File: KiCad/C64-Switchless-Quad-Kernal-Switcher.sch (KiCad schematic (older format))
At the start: 9 parts, among them J1 Pinlist_12pin, J2 Pinlist_12pin, J3 27C256_28PDIP, J4 Wireconnections, U1 ATtiny85-20PU

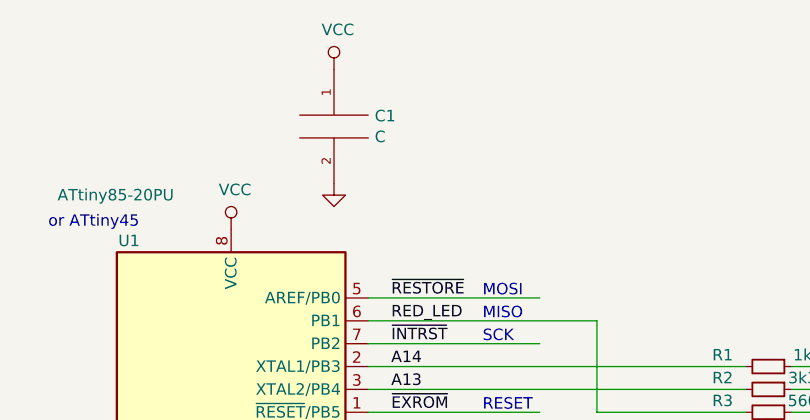
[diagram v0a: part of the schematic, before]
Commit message: firmware updates: use eprom, exromreset, opencollector
opencollector-ish means set reset and exrom as input when inactive.
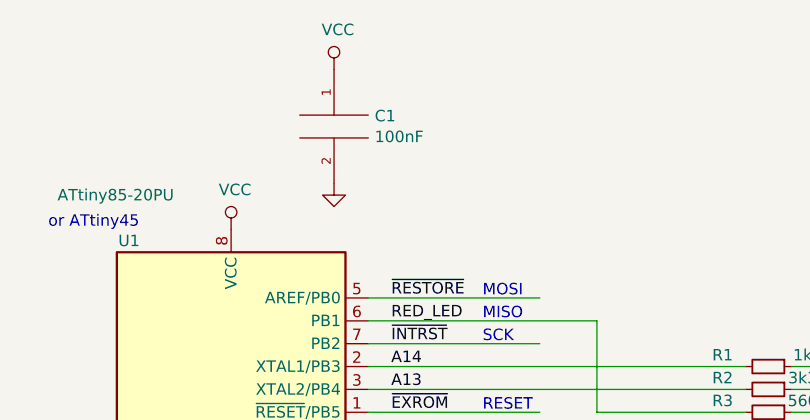
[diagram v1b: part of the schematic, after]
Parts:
- C1: value C -> 100nF
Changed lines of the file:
@@
 Sheet 1 1
 Title "C64 Switchless Quad Kernal Switcher (SKS64)"
-Date "2019-07-13"
+Date "2019-07-15"
 Rev "1.20"
 Comp "Bwack"
@@
 P 5350 4050
 F 0 "C1" H 5528 4096 50  0000 L CNN
-F 1 "C" H 5528 4005 50  0000 L CNN
+F 1 "100nF" H 5528 4005 50  0000 L CNN
 F 2 "Capacitor_THT:C_Disc_D3.8mm_W2.6mm_P2.50mm" H 5350 4050 50  0001 C CNN
 F 3 "~" H 5350 4050 50  0001 C CNN
